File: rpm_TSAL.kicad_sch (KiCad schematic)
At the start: 6 parts, among them J1 Conn_01x02, J2 Conn_01x02, J5 Conn_01x02, U1 ADUM5202WCRWZ, U2 ADUM5202WCRWZ

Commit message: added OPA and HV Resistors
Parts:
- removed U1, U2: ADUM5202WCRWZ, RW_16_ADI, symbol ADUM5202:ADUM5202WCRWZ
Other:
- sheet TSAL_RED ports: added TSAL_RED_OUT; removed none
- moved on the sheet: U3
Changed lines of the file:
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@@
+	(wire
+		(pts
+			(xy 62.23 139.7) (xy 73.66 139.7)
+		)
+		(stroke
+			(width 0)
+			(type default)
+		)
+	)
 	(wire
 		(pts
@@
 	(symbol
 		(lib_id "Zettler:AZ9371")
-		(at -43.18 184.15 0)
+		(at 34.29 165.1 0)
 		(unit 1)
 		(exclude_from_sim no)
@@
 		(dnp no)
 		(property "Reference" "U3"
-			(at -38.1 183.642 0)
+			(at 39.37 164.592 0)
 			(effects
 				(font
@@
 		)
 		(property "Value" "~"
-			(at -38.1 184.15 0)
+			(at 39.37 165.1 0)
 			(effects
 				(font
@@
 		)
 		(property "Footprint" "Zettler:AZ9371"
-			(at -43.18 184.15 0)
+			(at 34.29 165.1 0)
 			(effects
 				(font
@@
 		)
 		(property "Datasheet" ""
-			(at -43.18 184.15 0)
+			(at 34.29 165.1 0)
 			(effects
 				(font
@@
 		)
 		(property "Description" ""
-			(at -43.18 184.15 0)
+			(at 34.29 165.1 0)
 			(effects
 				(font
@@
 	)
 	(symbol
-		(lib_id "ADUM5202:ADUM5202WCRWZ")
-		(at -86.36 46.99 0)
-		(unit 1)
-		(exclude_from_sim no)
-		(in_bom yes)
-		(on_board yes)
-		(dnp no)
-		(property "Reference" "U2"
-			(at -74.168 42.926 0)
-			(effects
-				(font
-					(size 1.524 1.524)
-				)
-			)
-		)
-		(property "Value" "ADUM5202WCRWZ"
-			(at -74.168 45.466 0)
-			(effects
-				(font
-					(size 1.524 1.524)
-				)
-			)
-		)
-		(property "Footprint" "RW_16_ADI"
-			(at -86.36 46.99 0)
-			(effects
-				(font
-					(size 1.27 1.27)
-					(italic yes)
-				)
-				(hide yes)
-			)
-		)
-		(property "Datasheet" "ADUM5202WCRWZ"
-			(at -86.36 46.99 0)
-			(effects
-				(font
-					(size 1.27 1.27)
-					(italic yes)
-				)
-				(hide yes)
-			)
-		)
-		(property "Description" ""
-			(at -86.36 46.99 0)
-			(effects
-				(font
-					(size 1.27 1.27)
-				)
-				(hide yes)
-			)
-		)
-		(pin "14"
-		)
-		(pin "8"
-		)
-		(pin "15"
-		)
-		(pin "7"
-		)
-		(pin "12"
-		)
-		(pin "2"
-		)
-		(pin "1"
-		)
-		(pin "13"
-		)
-		(pin "4"
-		)
-		(pin "9"
-		)
-		(pin "5"
-		)
-		(pin "10"
-		)
-		(pin "3"
-		)
-		(pin "11"
-		)
-		(pin "16"
-		)
-		(pin "6"
-		)
-		(instances
-			(project "rpm_TSAL"
-				(path "/d61aec95-1a95-4bdc-98ef-7f05cebfb826"
-					(reference "U2")
-					(unit 1)
-				)
-			)
-		)
-	)
-	(symbol
 		(lib_id "Connector_Generic:Conn_01x02")
 		(at 52.07 63.5 0)
@@
 				(path "/d61aec95-1a95-4bdc-98ef-7f05cebfb826"
 					(reference "J5")
-					(unit 1)
-				)
-			)
-		)
-	)
-	(symbol
-		(lib_name "ADUM5202WCRWZ_1")
-		(lib_id "ADUM5202:ADUM5202WCRWZ")
-		(at -86.36 99.06 0)
-		(unit 1)
-		(exclude_from_sim no)
-		(in_bom yes)
-		(on_board yes)
-		(dnp no)
-		(property "Reference" "U1"
-			(at -74.168 94.234 0)
-			(effects
-				(font
-					(size 1.524 1.524)
-				)
-			)
-		)
-		(property "Value" "ADUM5202WCRWZ"
-			(at -74.168 96.774 0)
-			(effects
-				(font
-					(size 1.524 1.524)
-				)
-			)
-		)
-		(property "Footprint" "RW_16_ADI"
-			(at -86.36 99.06 0)
-			(effects
-				(font
-					(size 1.27 1.27)
-					(italic yes)
-				)
-				(hide yes)
-			)
-		)
-		(property "Datasheet" "ADUM5202WCRWZ"
-			(at -86.36 99.06 0)
-			(effects
-				(font
-					(size 1.27 1.27)
-					(italic yes)
-				)
-				(hide yes)
-			)
-		)
-		(property "Description" ""
-			(at -86.36 99.06 0)
-			(effects
-				(font
-					(size 1.27 1.27)
-				)
-				(hide yes)
-			)
-		)
-		(pin "14"
-		)
-		(pin "8"
-		)
-		(pin "15"
-		)
-		(pin "7"
-		)
-		(pin "12"
-		)
-		(pin "2"
-		)
-		(pin "1"
-		)
-		(pin "13"
-		)
-		(pin "4"
-		)
-		(pin "9"
-		)
-		(pin "5"
-		)
-		(pin "10"
-		)
-		(pin "3"
-		)
-		(pin "11"
-		)
-		(pin "16"
-		)
-		(pin "6"
-		)
-		(instances
-			(project ""
-				(path "/d61aec95-1a95-4bdc-98ef-7f05cebfb826"
-					(reference "U1")
 					(unit 1)
 				)
@@
 		)
 		(pin "TSAL_LED_RED" input
-			(at 73.66 135.89 180)
+			(at 73.66 139.7 180)
 			(effects
 				(font
@@
 			)
 		)
+		(pin "TSAL_RED_OUT" output
+			(at 61.595 139.7 0)
+			(effects
+				(font
+					(size 1.27 1.27)
+				)
+				(justify right)
+			)
+		)

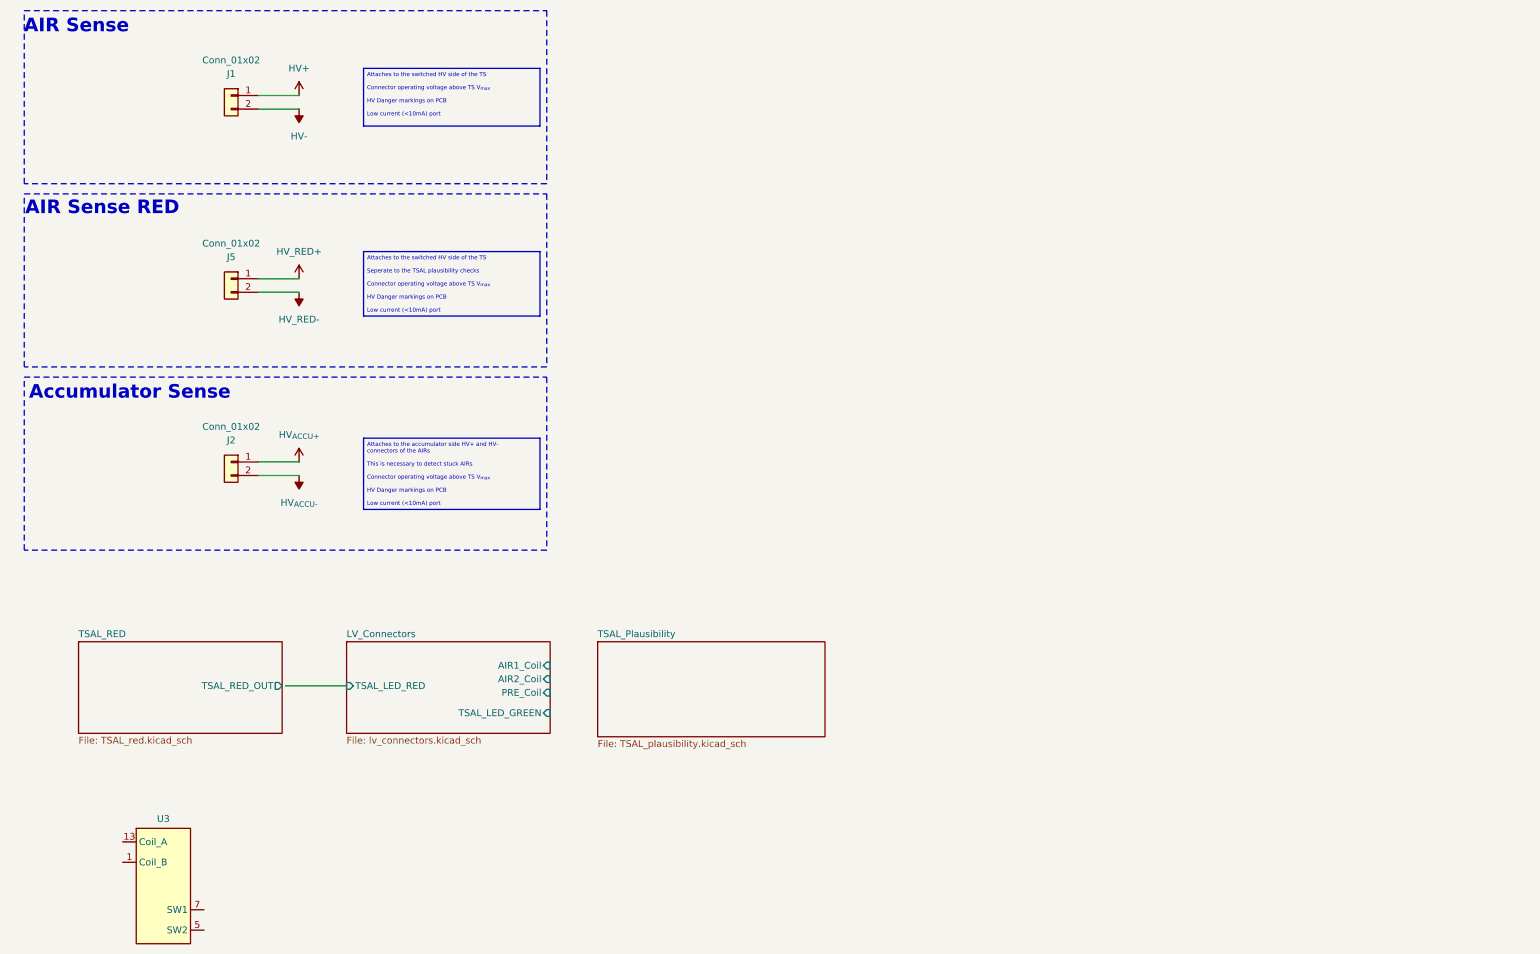
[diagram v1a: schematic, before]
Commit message: Changes to Pinout pending
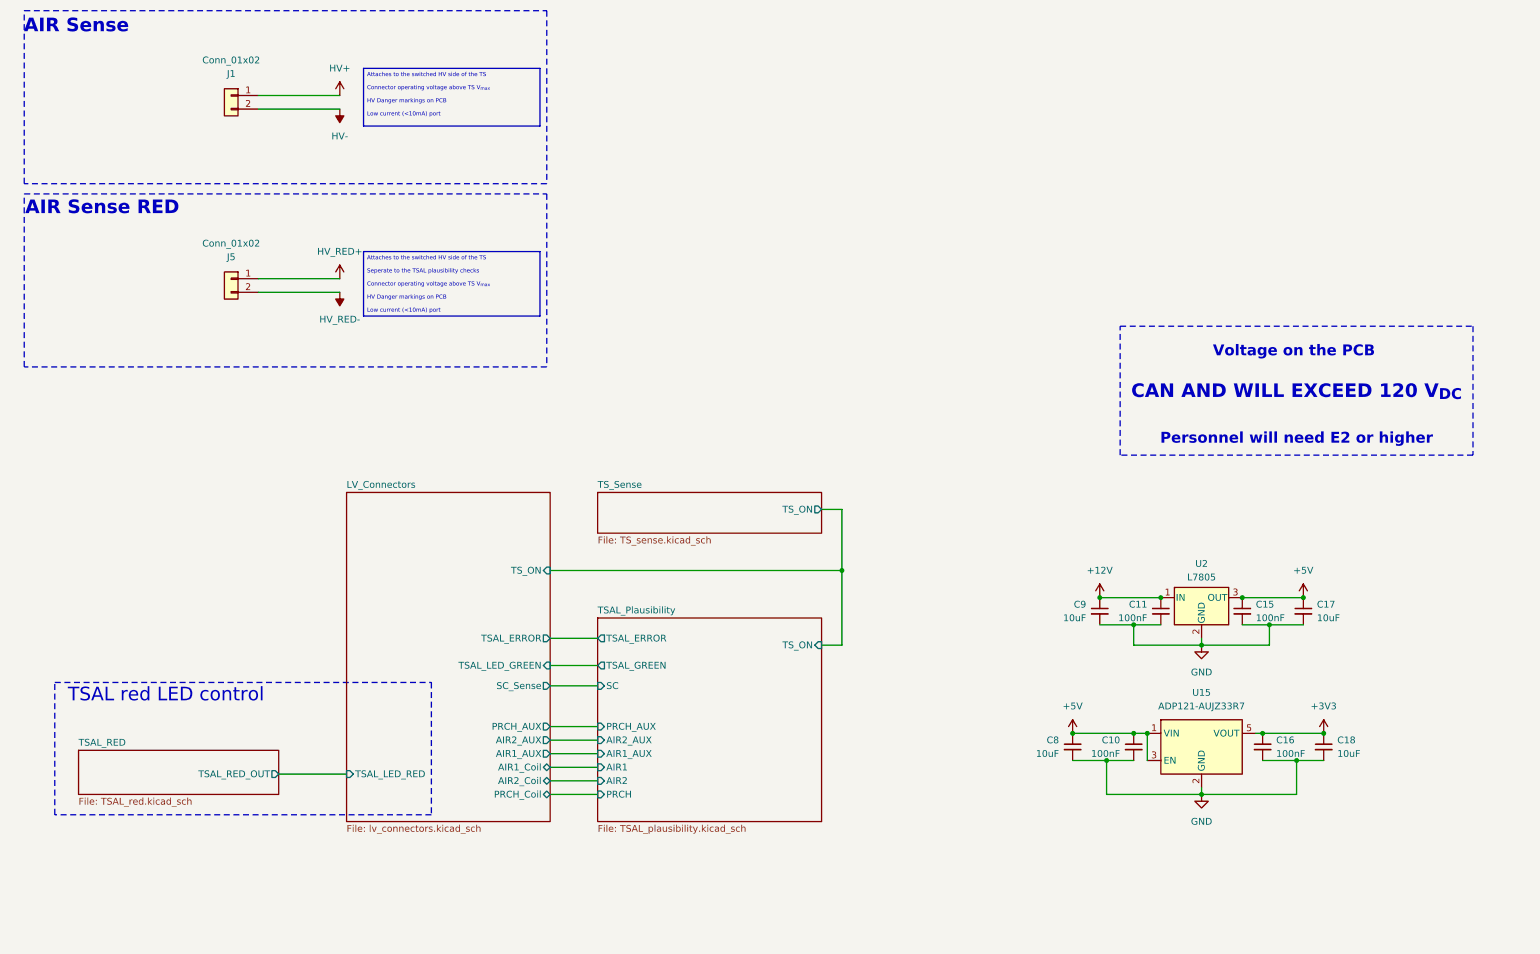
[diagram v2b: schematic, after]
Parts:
- removed J2: Conn_01x02, wuerth_conn:657002130101, symbol Connector_Generic:Conn_01x02
- removed U3: ~, Zettler:AZ9371, symbol Zettler:AZ9371
- added C10, C11, C15, C16: 100nF, Capacitor_SMD:C_0603_1608Metric, symbol Device:C_Small
- added C17, C18, C8, C9: 10uF, Capacitor_SMD:C_0603_1608Metric, symbol Device:C_Small
- added U15: ADP121-AUJZ33R7, Package_TO_SOT_SMD:TSOT-23-5, symbol Regulator_Linear:ADP7142AUJZ-3.3
- added U2: L7805, Package_TO_SOT_SMD:TO-252-2, symbol Regulator_Linear:L7805
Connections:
- new net +12V: C11.1, C9.1, U2.1 (IN)
- new net +3V3: C16.1, C18.1, U15.5 (VOUT)
- new net +5V: C10.1, C15.1, C17.1, C8.1, U15.1 (VIN), U15.3 (EN), U2.3 (OUT)
- new net GND: C10.2, C11.2, C15.2, C16.2, C17.2, C18.2, C8.2, C9.2, U15.2 (GND), U2.2 (GND)
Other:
- added sheet TS_Sense (TS_sense.kicad_sch)
- sheet LV_Connectors ports: added AIR1_AUX, AIR2_AUX, PRCH_AUX, PRCH_Coil, SC_Sense, TSAL_ERROR, TS_ON; removed PRE_Coil
- sheet TSAL_Plausibility ports: added AIR1, AIR1_AUX, AIR2, AIR2_AUX, PRCH, PRCH_AUX, SC, TSAL_ERROR, TSAL_GREEN, TS_ON; removed none
- note added: "TSAL red LED control"
- note removed: "Accumulator Sense"

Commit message: Changed Layout
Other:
- sheet LV_Connectors ports: added SC; removed SC_Sense
- sheet TSAL_RED ports: added TS+, TS-; removed none
- sheet TS_Sense ports: added TS+, TS-; removed none
- note added: "TS Sense Connector"
- note added: "TS Sense RED Connector"
- note removed: "AIR Sense"
- note removed: "AIR Sense RED"
- note removed: "TSAL red LED control"
- moved on the sheet: C11, C15, C17, C9, J1, J5, U2

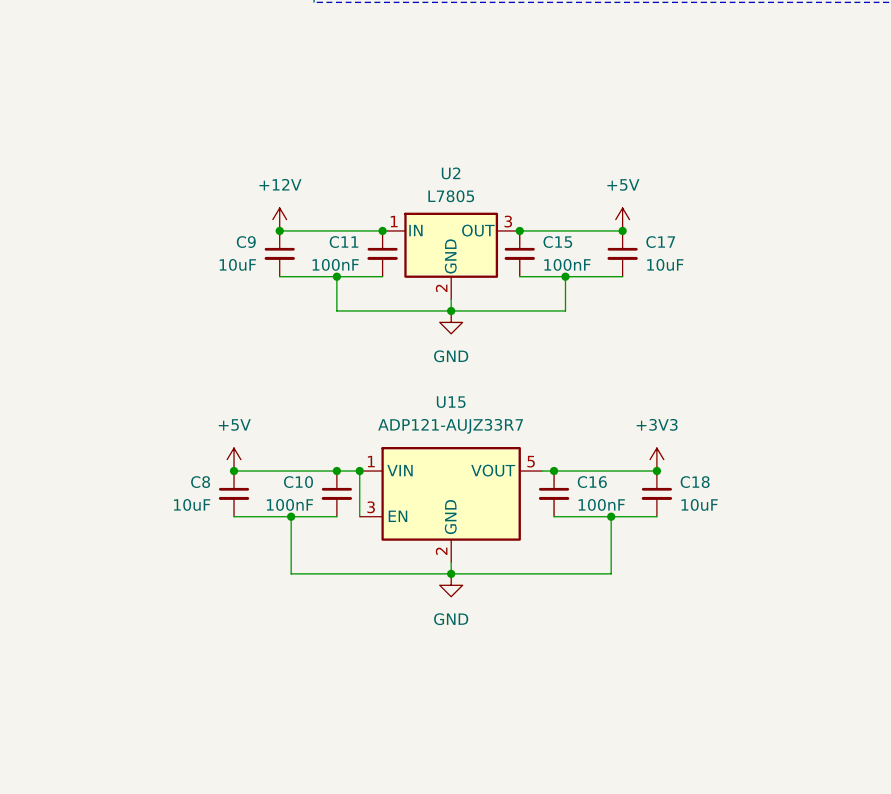
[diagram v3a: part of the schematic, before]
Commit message: Checked Rules. Looks good. Need to fix AIR Aux detection. Need to Fix Coil Activation. Need to add SCS Failure Output and SCS Failure Inhibiter
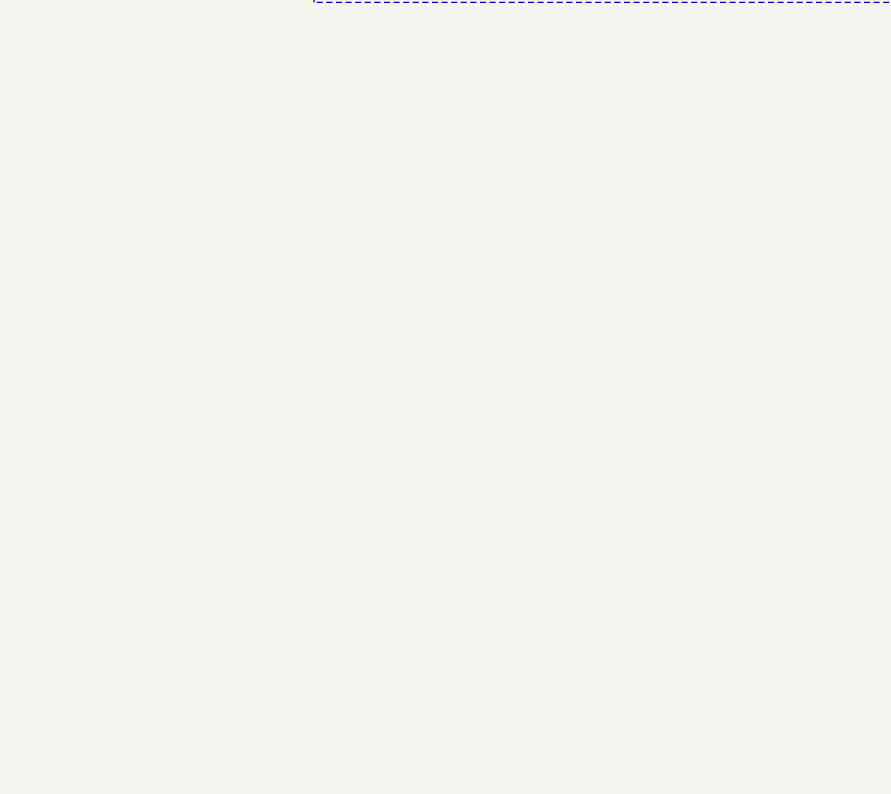
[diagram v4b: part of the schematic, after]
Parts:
- removed C10, C11, C15, C16: 100nF, Capacitor_SMD:C_0603_1608Metric, symbol Device:C_Small
- removed C17, C18, C8, C9: 10uF, Capacitor_SMD:C_0603_1608Metric, symbol Device:C_Small
- removed U15: ADP121-AUJZ33R7, Package_TO_SOT_SMD:TSOT-23-5, symbol Regulator_Linear:ADP7142AUJZ-3.3
- removed U2: L7805, Package_TO_SOT_SMD:TO-252-2, symbol Regulator_Linear:L7805
